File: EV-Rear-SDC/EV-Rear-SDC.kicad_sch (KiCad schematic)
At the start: 63 parts, among them J1 JST-XA, J2 Conn_01x06, J3 Conn_01x08, J4 Conn_01x05, J5 Conn_01x14, K1 Relay_SPDT_G6RN, Q1 BSS205N, Q2 BSS205N, Q3 BSS205N, Q4 BSS205N, Q5 BSS205N, Q6 BSS205N, Q7 BSS205N, Q8 BSS205N, Q9 BSS205N, U1 SCH16T-K01-10, U3 MAX3390EEUD_T

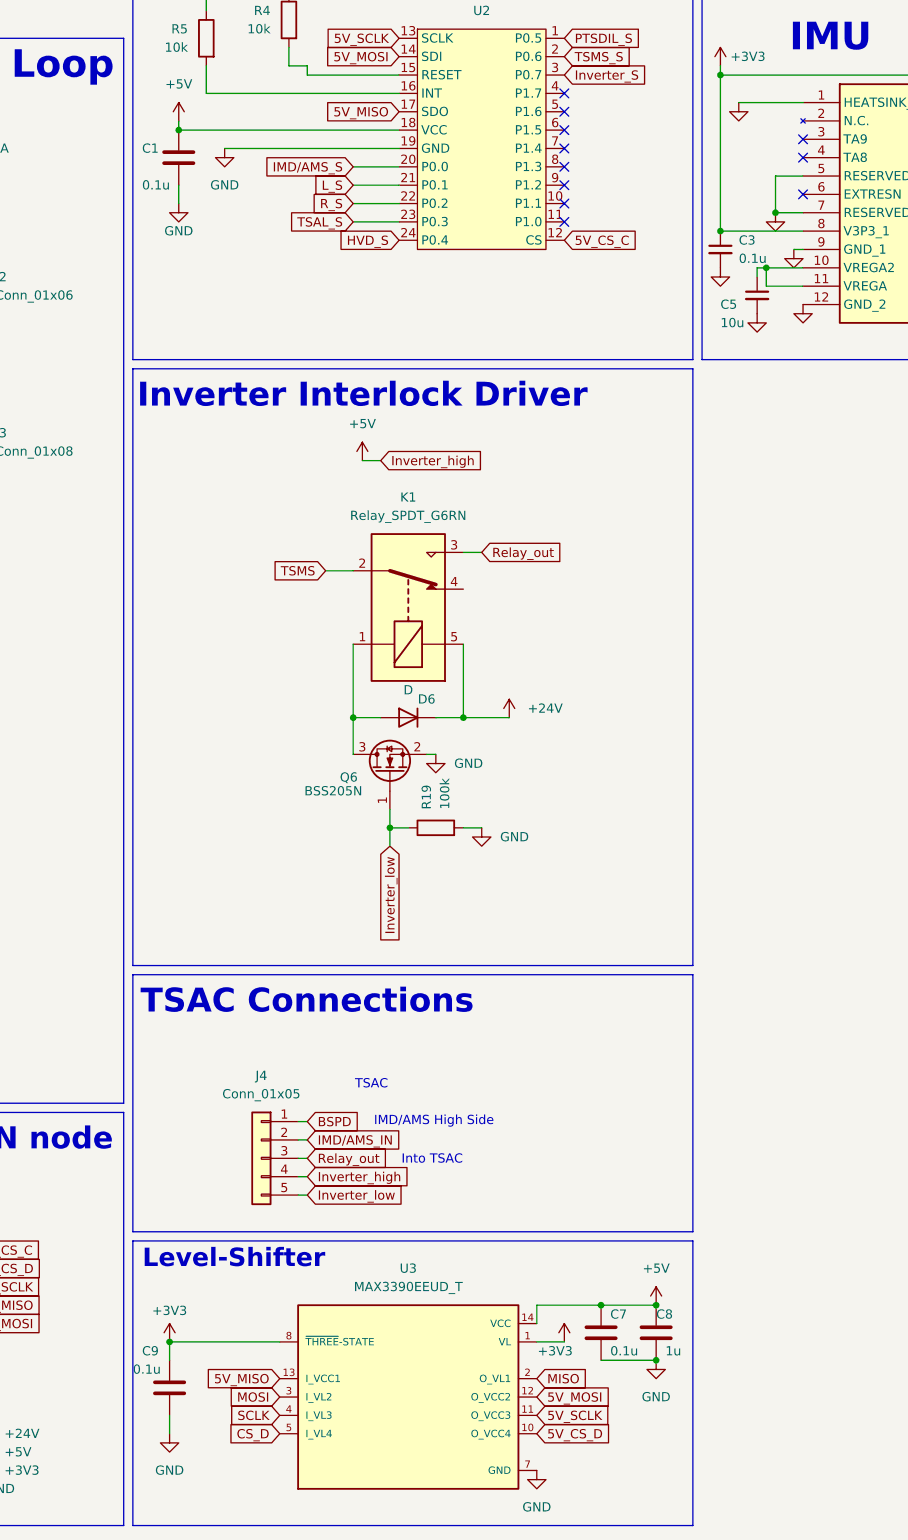
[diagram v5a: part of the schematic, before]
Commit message: Added stuff to BOM
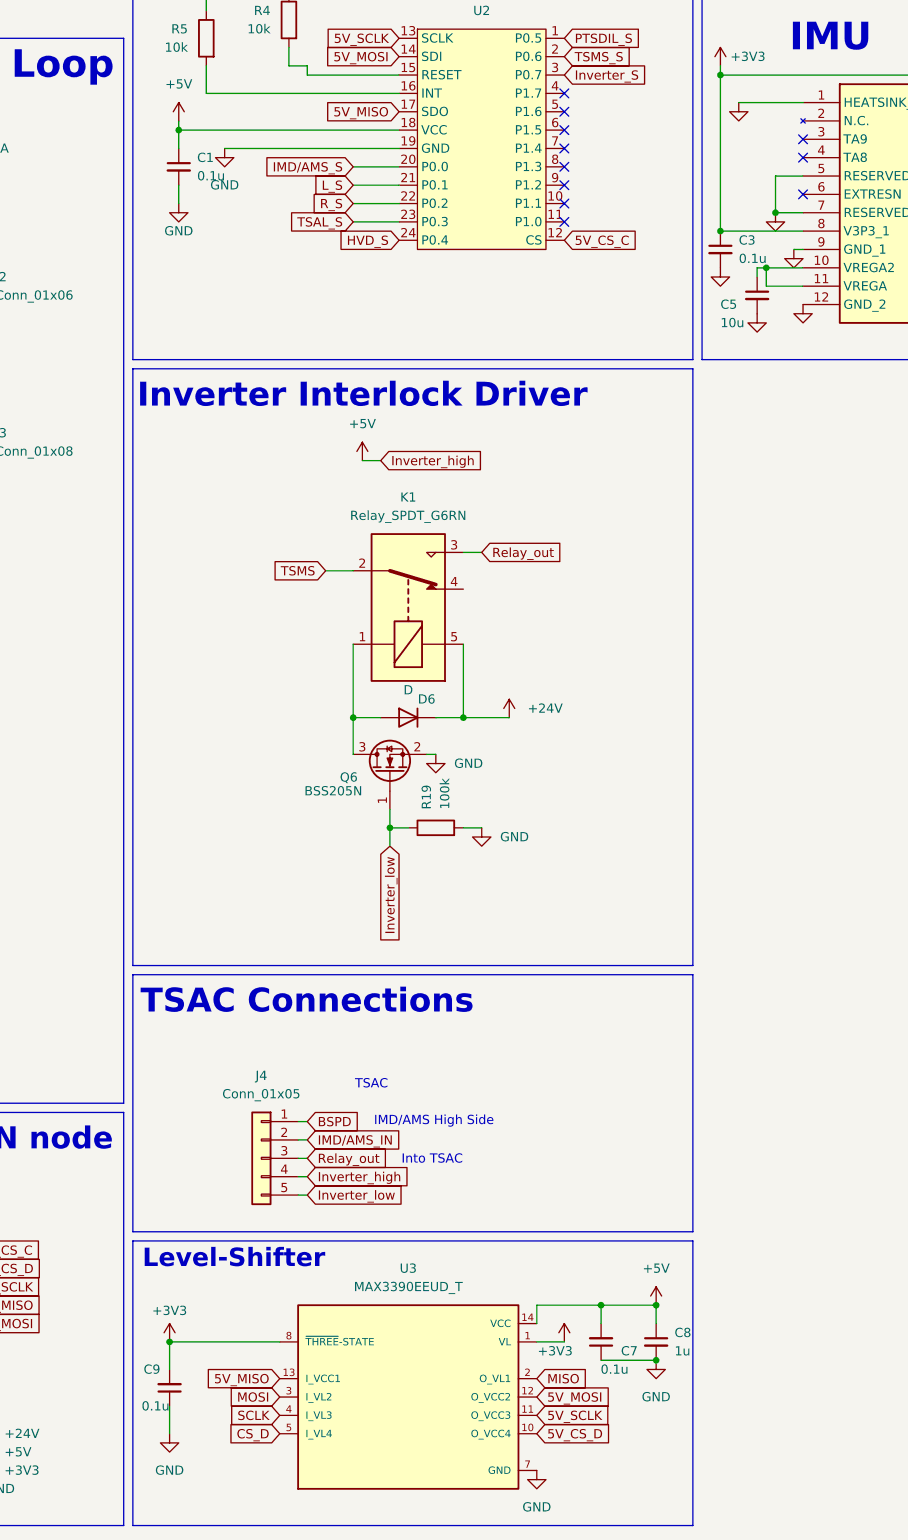
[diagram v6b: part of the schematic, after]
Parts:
- removed C1, C7, C9: 0.1u, Capacitor_SMD:C_0805_2012Metric, symbol Device:C
- removed C8: 1u, Capacitor_SMD:C_0805_2012Metric, symbol Device:C
- added C1, C7, C9: 0.1u, Capacitor_SMD:C_0805_2012Metric, symbol Device:C_Small
- added C8: 1u, Capacitor_SMD:C_0805_2012Metric, symbol Device:C_Small
- C2, C3: MFP (none) -> GA0805Y104JXABT31G; S1PL (none) -> https://www.mouser.co.uk/en/ProductDetail/Vishay-Vitramon/G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; S1PN (none) -> 77-GA805Y104JXABT31G; S1PRICE (none) -> 0.37; S2PL (none) -> https://www.digikey.co.uk/en/products/detail/vishay-vitramo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; S2PN (none) -> 720-GA0805Y104JXABT31GCT-ND; S2PRICE (none) -> 0.368
- C4, C6: MFP (none) -> VJ0805Y105KXQTW1BC; S1PL (none) -> https://www.mouser.co.uk/en/ProductDetail/Vishay-Vitramon/V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; S1PN (none) -> 77-VJ0805Y105KXQTBC; S1PRICE (none) -> 0.196; S2PL (none) -> https://www.digikey.co.uk/en/products/detail/vishay-vitramo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; S2PN (none) -> 720-1757-1-ND; S2PRICE (none) -> 0.160
- C5: MFP (none) -> VJ0805Y106KXQTW1BC; S1PL (none) -> https://www.mouser.co.uk/en/ProductDetail/Vishay-Vitramon/V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; S1PN (none) -> 77-VJ0805Y106KXQTWBC; S1PRICE (none) -> 0.361; S2PL (none) -> https://www.digikey.co.uk/en/products/detail/vishay-vitramo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; S2PN (none) -> 720-VJ0805Y106KXQTW1BCTR-ND; S2PRICE (none) -> 0.38
- J2: S1PL https://www.mouser.co.uk/en/ProductDetail/JST-Commercial/B0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 -> https://www.mouser.co.uk/en/ProductDetail/JST-Commercial/S0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
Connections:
- net +3V3: now also C9.2
- net +5V: now also C1.1, C7.2, C8.1
- net GND: now also C1.2, C7.1, C8.2, C9.1
